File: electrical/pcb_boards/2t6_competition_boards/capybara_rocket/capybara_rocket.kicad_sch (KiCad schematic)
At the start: 110 parts, among them J1 3.6V Battery, J10 Elevator, J11 SparkFun MAX-M10S, J12 Aileron 1, J13 Aileron 2, J14 Ground Camera, J15 Payload Camera, J16 DC Motor, J2 1.2V Battery, J3 3.6V Switch, J4 1.2V Switch, J5 LED, J6 NC, J7 CC, J8 VL53L1-SATEL, J9 Egg, Q1 SI4435DDY, Q2 SI4435DDY, U1 DS1307+, U10 TPS3839, U11 MP3414, U12 SN74LVC1G04, U13 MCP1640, U14 TPS3839, U15 STM32 NUCLEO-G431KB, U16 SN74AUP1G04, U17 SparkFun XBee Explorer, U2 Adafruit BNO085, U3 TLC555, U4 EEPROM, U5 LTC3536, U6 LTC3536, U7 Adafruit BMP581, U8 DRV8212, U9 INA219, Y1 AB38T-32.768KHZ

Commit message: New graphics and layout work
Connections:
- net 3.3V MCU: no longer R18.2, TP5.1
- net 5.5V: now also R18.2, TP5.1
- net CS: no longer U2.JP2_6 (CS)
- net MISO: no longer U2.JP1_5 (SDA)
- net MOSI: no longer U2.JP2_5 (DI)
- net SCL: now also J8.2, U2.JP1_4 (SCL); no longer J8.3
- net SCLK: no longer U2.JP1_4 (SCL)
- net SDA: now also J8.3, U2.JP1_5 (SDA); no longer J8.2
- no-connect marks 62 -> 64
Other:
- moved on the sheet: D5, R18, TP5
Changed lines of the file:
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@@
 	)
 	(no_connect
+		(at 22.86 171.45)
+	)
+	(no_connect
 		(at 29.21 71.12)
 	)
@@
 	)
 	(no_connect
+		(at 22.86 168.91)
+	)
+	(no_connect
 		(at 99.06 152.4)
 	)
@@
 		)
 	)
-	(global_label "MOSI"
-		(shape input)
-		(at 22.86 171.45 180)
-		(fields_autoplaced yes)
-		(effects
-			(font
-				(size 1.27 1.27)
-			)
-			(justify right)
-		)
-		(property "Intersheetrefs" "${INTERSHEET_REFS}"
-			(at 15.2786 171.45 0)
-			(effects
-				(font
-					(size 1.27 1.27)
-				)
-				(justify right)
-				(hide yes)
-			)
-		)
-	)
 	(global_label "SDA"
 		(shape bidirectional)
@@
 		)
 	)
-	(global_label "3.3V MCU"
+	(global_label "5.5V"
 		(shape input)
-		(at 194.31 193.04 180)
+		(at 193.04 193.04 180)
 		(fields_autoplaced yes)
 		(effects
@@
 		)
 		(property "Intersheetrefs" "${INTERSHEET_REFS}"
-			(at 182.1929 193.04 0)
+			(at 185.9424 193.04 0)
 			(effects
 				(font
@@
 		)
 	)
+	(global_label "SCL"
+		(shape bidirectional)
+		(at 90.17 130.81 270)
+		(fields_autoplaced yes)
+		(effects
+			(font
+				(size 1.27 1.27)
+			)
+			(justify right)
+		)
+		(property "Intersheetrefs" "${INTERSHEET_REFS}"
+			(at 90.17 138.4141 90)
+			(effects
+				(font
+					(size 1.27 1.27)
+				)
+				(justify right)
+				(hide yes)
+			)
+		)
+	)
 	(global_label "SDA"
 		(shape bidirectional)
@@
 		)
 	)
-	(global_label "SDA"
-		(shape bidirectional)
-		(at 90.17 130.81 270)
-		(fields_autoplaced yes)
-		(effects
-			(font
-				(size 1.27 1.27)
-			)
-			(justify right)
-		)
-		(property "Intersheetrefs" "${INTERSHEET_REFS}"
-			(at 90.17 138.4746 90)
-			(effects
-				(font
-					(size 1.27 1.27)
-				)
-				(justify right)
-				(hide yes)
-			)
-		)
-	)
 	(global_label "NC_REL"
 		(shape output)
@@
 		)
 	)
-	(global_label "CS"
-		(shape input)
-		(at 22.86 168.91 180)
-		(fields_autoplaced yes)
-		(effects
-			(font
-				(size 1.27 1.27)
-			)
-			(justify right)
-		)
-		(property "Intersheetrefs" "${INTERSHEET_REFS}"
-			(at 17.3953 168.91 0)
-			(effects
-				(font
-					(size 1.27 1.27)
-				)
-				(justify right)
-				(hide yes)
-			)
-		)
-	)
 	(global_label "AILERON"
 		(shape input)
@@
 		)
 	)
-	(global_label "MISO"
-		(shape output)
-		(at 22.86 176.53 180)
-		(fields_autoplaced yes)
-		(effects
-			(font
-				(size 1.27 1.27)
-			)
-			(justify right)
-		)
-		(property "Intersheetrefs" "${INTERSHEET_REFS}"
-			(at 15.2786 176.53 0)
-			(effects
-				(font
-					(size 1.27 1.27)
-				)
-				(justify right)
-				(hide yes)
-			)
-		)
-	)
 	(global_label "3.3V MCU"
 		(shape output)
@@
 		)
 	)
+	(global_label "SDA"
+		(shape bidirectional)
+		(at 22.86 176.53 180)
+		(fields_autoplaced yes)
+		(effects
+			(font
+				(size 1.27 1.27)
+			)
+			(justify right)
+		)
+		(property "Intersheetrefs" "${INTERSHEET_REFS}"
+			(at 15.1954 176.53 0)
+			(effects
+				(font
+					(size 1.27 1.27)
+				)
+				(justify right)
+				(hide yes)
+			)
+		)
+	)
 	(global_label "INV_PWM_1"
 		(shape input)
@@
 		)
 	)
+	(global_label "SCL"
+		(shape bidirectional)
+		(at 22.86 173.99 180)
+		(fields_autoplaced yes)
+		(effects
+			(font
+				(size 1.27 1.27)
+			)
+			(justify right)
+		)
+		(property "Intersheetrefs" "${INTERSHEET_REFS}"
+			(at 15.2559 173.99 0)
+			(effects
+				(font
+					(size 1.27 1.27)
+				)
+				(justify right)
+				(hide yes)
+			)
+		)
+	)
 	(global_label "DC_PWM_1"
 		(shape input)
@@
 		)
 	)
-	(global_label "SCLK"
-		(shape input)
-		(at 22.86 173.99 180)
+	(global_label "SDA"
+		(shape bidirectional)
+		(at 87.63 130.81 270)
 		(fields_autoplaced yes)
 		(effects
@@
 		)
 		(property "Intersheetrefs" "${INTERSHEET_REFS}"
-			(at 15.0972 173.99 0)
+			(at 87.63 138.4746 90)
 			(effects
 				(font
@@
 		)
 	)
-	(global_label "SCL"
-		(shape bidirectional)
-		(at 87.63 130.81 270)
-		(fields_autoplaced yes)
-		(effects
-			(font
-				(size 1.27 1.27)
-			)
-			(justify right)
-		)
-		(property "Intersheetrefs" "${INTERSHEET_REFS}"
-			(at 87.63 138.4141 90)
-			(effects
-				(font
-					(size 1.27 1.27)
-				)
-				(justify right)
-				(hide yes)
-			)
-		)
-	)
 	(global_label "G_CAM_OUT"
 		(shape input)
@@
 	(symbol
 		(lib_id "Device:R")
-		(at 198.12 193.04 270)
+		(at 196.85 193.04 270)
 		(unit 1)
 		(exclude_from_sim no)
@@
 		(dnp no)
 		(property "Reference" "R18"
-			(at 198.12 190.246 90)
+			(at 196.85 190.246 90)
 			(effects
 				(font
@@
 		)
 		(property "Value" "100Ω"
-			(at 198.12 195.834 90)
+			(at 196.85 195.834 90)
 			(effects
 				(font
@@
 		)
 		(property "Footprint" "Resistor_SMD:R_0603_1608Metric_Pad0.98x0.95mm_HandSolder"
-			(at 198.12 191.262 90)
+			(at 196.85 191.262 90)
 			(effects
 				(font
@@
 		)
 		(property "Datasheet" "~"
-			(at 198.12 193.04 0)
+			(at 196.85 193.04 0)
 			(effects
 				(font
@@
 		)
 		(property "Description" "Resistor"
-			(at 198.12 193.04 0)
+			(at 196.85 193.04 0)
 			(effects
 				(font
@@
 	(symbol
 		(lib_id "power:GND")
-		(at 209.55 193.04 90)
+		(at 208.28 193.04 90)
 		(unit 1)
 		(exclude_from_sim no)
@@
 		(dnp no)
 		(property "Reference" "#PWR053"
-			(at 215.9 193.04 0)
+			(at 214.63 193.04 0)
 			(effects
 				(font
@@
 		)
 		(property "Value" "GND"
-			(at 212.598 193.04 90)
+			(at 211.328 193.04 90)
 			(effects
 				(font
@@
 		)
 		(property "Footprint" ""
-			(at 209.55 193.04 0)
+			(at 208.28 193.04 0)
 			(effects
 				(font
@@
 		)
 		(property "Datasheet" ""
-			(at 209.55 193.04 0)
+			(at 208.28 193.04 0)
 			(effects
 				(font
@@
 		)
 		(property "Description" "Power symbol creates a global label with name \"GND\" , ground"
-			(at 209.55 193.04 0)
+			(at 208.28 193.04 0)
 			(effects
 				(font
@@
 	(symbol
 		(lib_id "Device:LED")
-		(at 205.74 193.04 180)
+		(at 204.47 193.04 180)
 		(unit 1)
 		(exclude_from_sim no)
@@
 		(dnp no)
 		(property "Reference" "D5"
-			(at 205.74 190.246 0)
+			(at 204.47 190.246 0)
 			(effects
 				(font
@@
 		)
 		(property "Value" "LED"
-			(at 205.74 195.834 0)
+			(at 204.47 195.834 0)
 			(effects
 				(font
@@
 		)
 		(property "Footprint" "DigiKey:WL-SMCW_0603"
-			(at 205.74 193.04 0)
+			(at 204.47 193.04 0)
 			(effects
 				(font
@@
 		)
 		(property "Datasheet" "~"
-			(at 205.74 193.04 0)
+			(at 204.47 193.04 0)
 			(effects
 				(font
@@
 		)
 		(property "Description" "Light emitting diode"
-			(at 205.74 193.04 0)
+			(at 204.47 193.04 0)
 			(effects
 				(font
@@
 		)
 		(property "Sim.Pins" "1=K 2=A"
-			(at 205.74 193.04 0)
+			(at 204.47 193.04 0)
 			(effects
 				(font
@@
 	(symbol
 		(lib_id "Connector:TestPoint")
-		(at 194.31 193.04 0)
+		(at 193.04 193.04 0)
 		(unit 1)
 		(exclude_from_sim no)
@@
 		(dnp no)
 		(property "Reference" "TP5"
-			(at 193.04 187.96 0)
+			(at 191.77 187.96 0)
 			(effects
 				(font
@@
 		)
 		(property "Value" "TestPoint"
-			(at 193.04 189.992 0)
+			(at 191.77 189.992 0)
 			(effects
 				(font
@@
 		)
 		(property "Footprint" "TestPoint:TestPoint_THTPad_2.0x2.0mm_Drill1.0mm"
-			(at 199.39 193.04 0)
+			(at 198.12 193.04 0)
 			(effects
 				(font
@@
 		)
 		(property "Datasheet" "~"
-			(at 199.39 193.04 0)
+			(at 198.12 193.04 0)
 			(effects
 				(font
@@
 		)
 		(property "Description" "test point"
-			(at 194.31 193.04 0)
+			(at 193.04 193.04 0)
 			(effects
 				(font

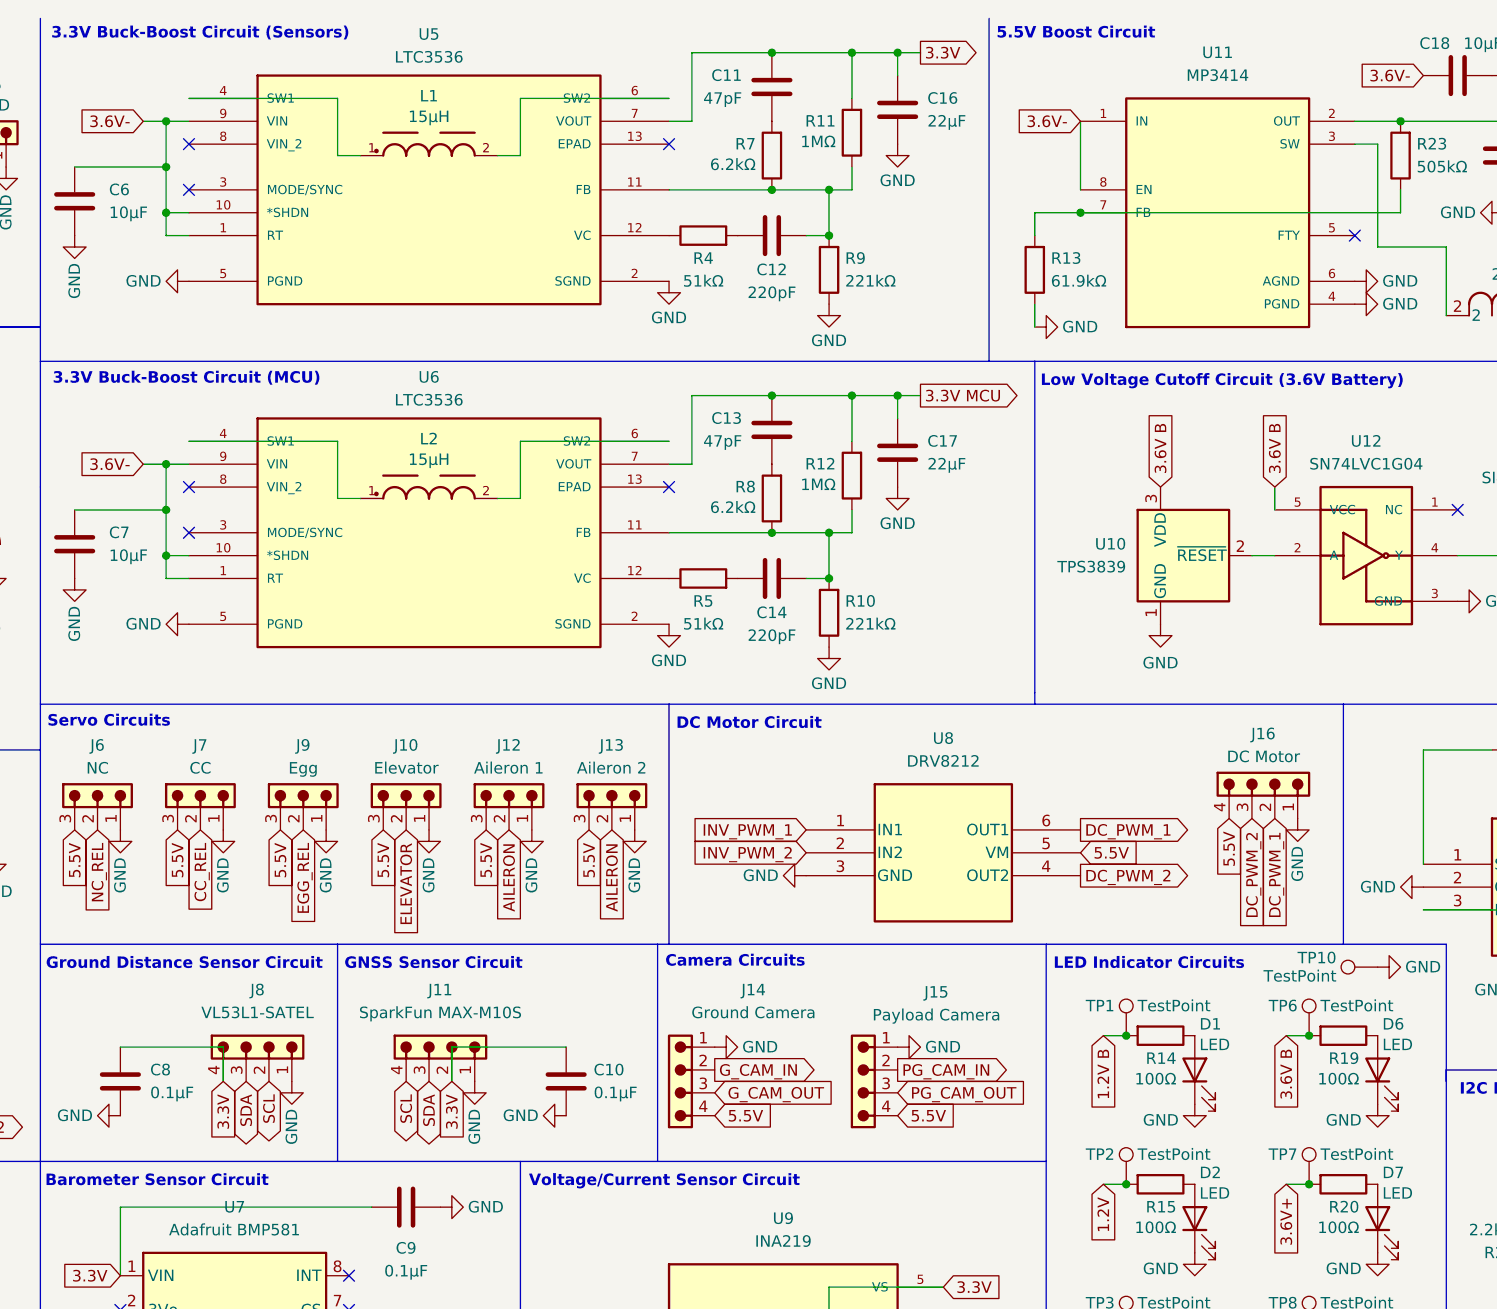
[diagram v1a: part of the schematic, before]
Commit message: Completed layout for CPL PCB
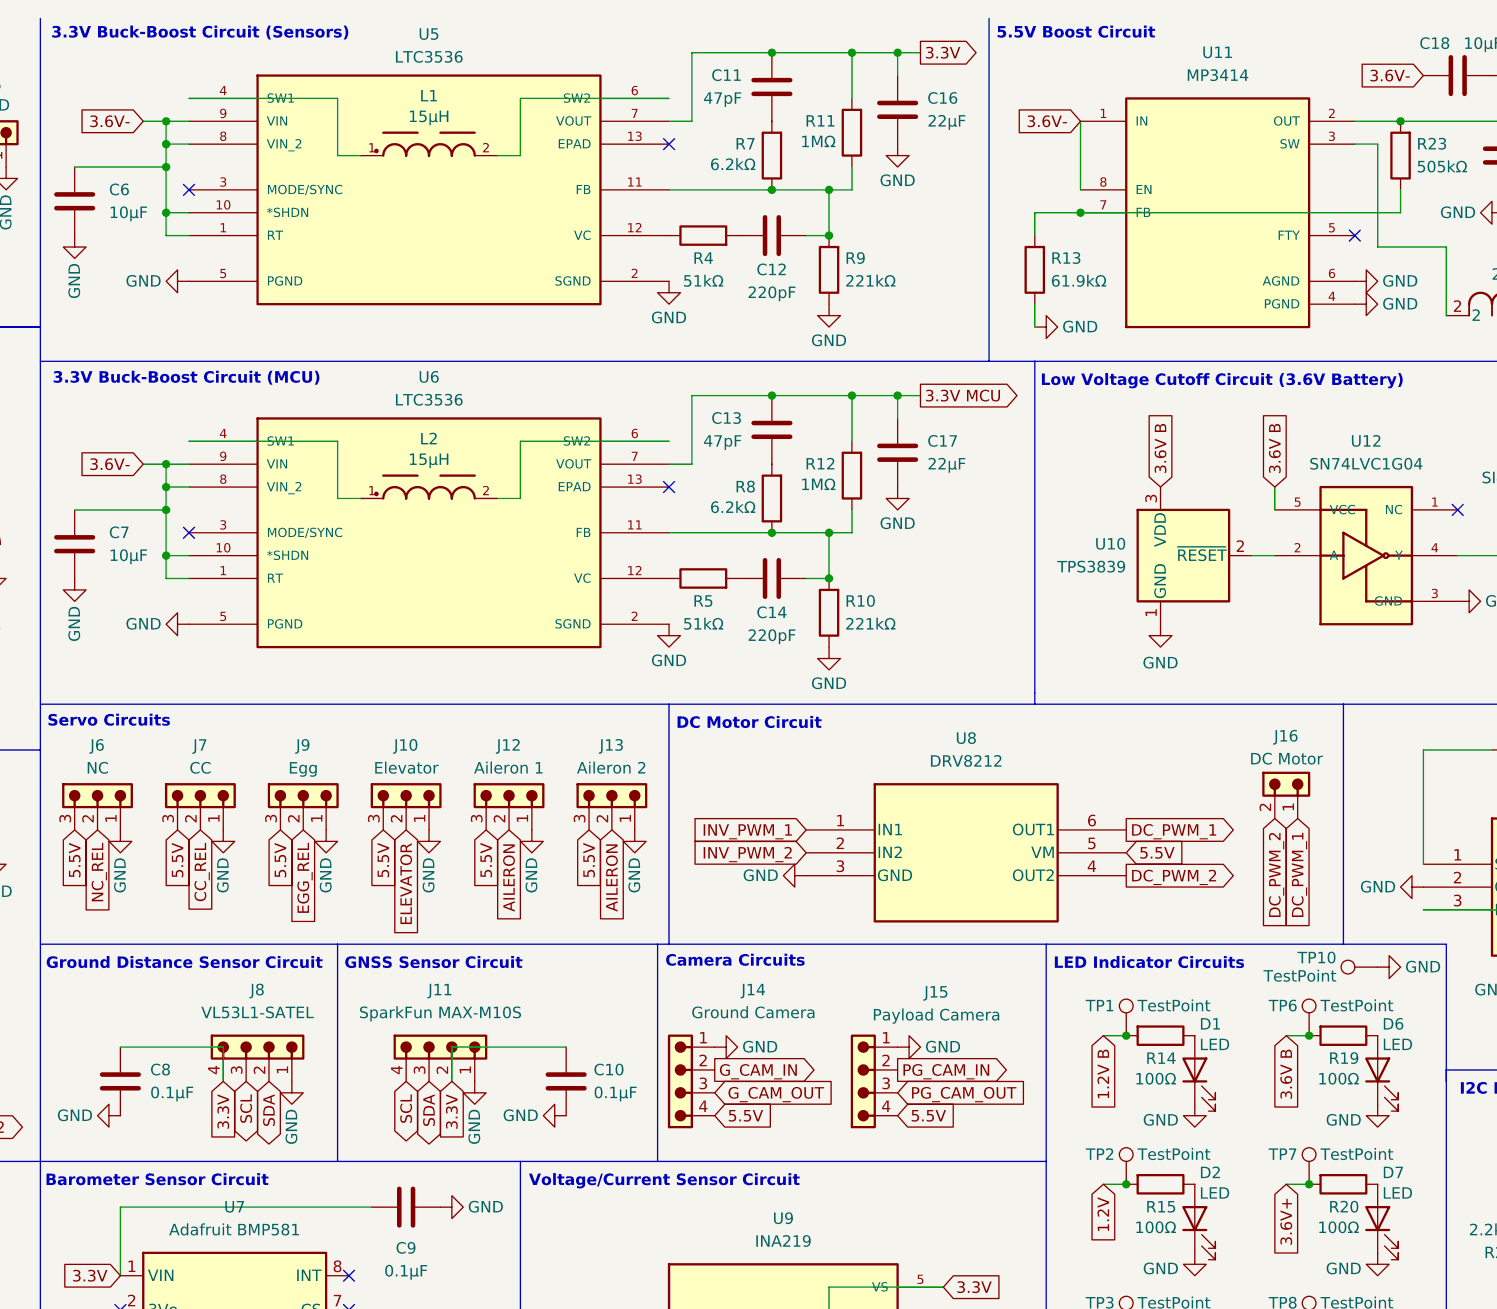
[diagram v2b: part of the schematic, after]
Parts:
- removed J16: DC Motor, RSX_CanSat_Custom_KiCad_Footprints:J_Wurth_WR-WTB_62000411622, symbol RSX_CanSat_Custom_KiCad_Symbols:Wurth_M4_62000411622
- added J16: DC Motor, RSX_CanSat_Custom_KiCad_Footprints:J_Wurth_WR-WTB_62000211622, symbol RSX_CanSat_Custom_KiCad_Symbols:Wurth_M2_62000211622
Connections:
- net 3.6V-: now also U5.8 (VIN_2), U6.8 (VIN_2)
- net DC_PWM_1: now also J16.1
- net DC_PWM_2: now also J16.2
- net SCL: now also J8.3; no longer J8.2
- net SDA: now also J8.2; no longer J8.3
- no-connect marks 64 -> 62
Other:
- moved on the sheet: U8

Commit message: cpl pcb schematic review complete
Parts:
- added C23, C25, C26, C27, C28, C29: 0.1μF, Capacitor_SMD:C_0805_2012Metric_Pad1.18x1.45mm_HandSolder, symbol Device:C
- added C24: 10μF, Capacitor_SMD:C_1206_3216Metric_Pad1.33x1.80mm_HandSolder, symbol Device:C
- R14, R15, R16, R17, R19, R20, R21, R22: value 100Ω -> 1kΩ
- R18: value 100Ω -> 1.5kΩ
- R24, R25: value 2.2kΩ -> 4.7kΩ
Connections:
- net 1.2V: now also Q2.6, Q2.7, Q2.8
- net 1.2V B: now also J4.1, Q2.2, Q2.3, C26.1, C29.1
- net 3.3V: now also J8.3, U2.JP2_4 (~{RST}), U2.JP2_6 (CS), U4.3 (*WP); no longer C8.1, J8.4
- net 3.3V MCU: now also U15.CN3_14 (3V3); no longer U15.CN3_1 (VIN)
- net 3.6V B: now also J3.1, Q1.2, Q1.3, C27.1, C28.1
- net 3.6V+: now also Q1.6, Q1.7, Q1.8
- net 5.5V: now also J10.2, J12.2, J13.2, J14.3, J15.3, J6.2, J7.2, J9.2, C23.1, C24.1; no longer J10.3, J12.3, J13.3, J14.4, J15.4, J6.3, J7.3, J9.3
- net AILERON: now also J12.1, J13.1; no longer J12.2, J13.2
- net CC_REL: now also J7.1; no longer J7.2
- net EGG_REL: now also J9.1; no longer J9.2
- net ELEVATOR: now also J10.1; no longer J10.2
- net GND: now also C8.1, J10.3, J12.3, J13.3, J14.4, J15.4, J6.3, J7.3, J8.4, J9.3, U2.JP2_2 (P0), U2.JP2_3 (P1), U2.JP2_5 (DI), U5.13 (EPAD), U5.3 (MODE/SYNC), U6.13 (EPAD), U6.3 (MODE/SYNC), U9.1 (A1), U9.2 (A0), C23.2, C24.2, C25.2, C26.2, C27.2, C28.2, C29.2; no longer J10.1, J12.1, J13.1, J14.1, J15.1, J3.1, J4.1, J6.1, J7.1, J8.1, J9.1, U4.3 (*WP)
- net G_CAM_OUT: now also J14.1; no longer J14.3
- net NC_REL: now also J6.1; no longer J6.2
- net PG_CAM_OUT: now also J15.1; no longer J15.3
- net SCL: now also J8.1; no longer J8.3
- net INT: now reaches U2.JP1_6 (~{INT})
- net INT: now also U15.CN3_15 (T_SWO(PB3/PB8(D13)))
- no-connect marks 62 -> 39
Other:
- note added: "change the 15uH VOTH ltc3536 inductors to"
- note added: "https://www.digikey.ca/en/products/detail/tai-tech-advanced-electronics-co-ltd/HPC-8040NC-4R7M/17835630"
- moved on the sheet: D6, D7, J16, R19, R20, TP1, TP10, TP2, TP6, TP7
